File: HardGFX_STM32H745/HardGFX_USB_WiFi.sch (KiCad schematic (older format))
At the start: 24 parts, among them J1 UART, J7 47590-0001, J8 JTAG, J9 Boot Option, Q1 BSR14, SW1 SW_MEC_5E, U10 ESP32-WROOM-32E_(4MB), U8 STMPS2151STR, U9 USBLC6-4SC6

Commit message: Add Info folder that contain data about reference design, datasheet component of references.
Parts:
- U10: Digikey# (none) -> 1965-ESP32-WROOM-32E(4MBHIGHTEMP)TR-ND; Manf# (none) -> ESP32-WROOM-32E (4MB HIGH TEMP)
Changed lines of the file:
@@
 F 6 "1.1" H 3350 4000 50  0001 L BNN "PARTREV"
 F 7 "3.25mm" H 3350 4000 50  0001 L BNN "MAXIMUM_PACKAGE_HEIGHT"
+F 8 "1965-ESP32-WROOM-32E(4MBHIGHTEMP)TR-ND" H 3350 4000 50  0001 C CNN "Digikey#"
+F 9 "ESP32-WROOM-32E (4MB HIGH TEMP)" H 3350 4000 50  0001 C CNN "Manf#"
 	1    3350 4000
 	1    0    0    -1

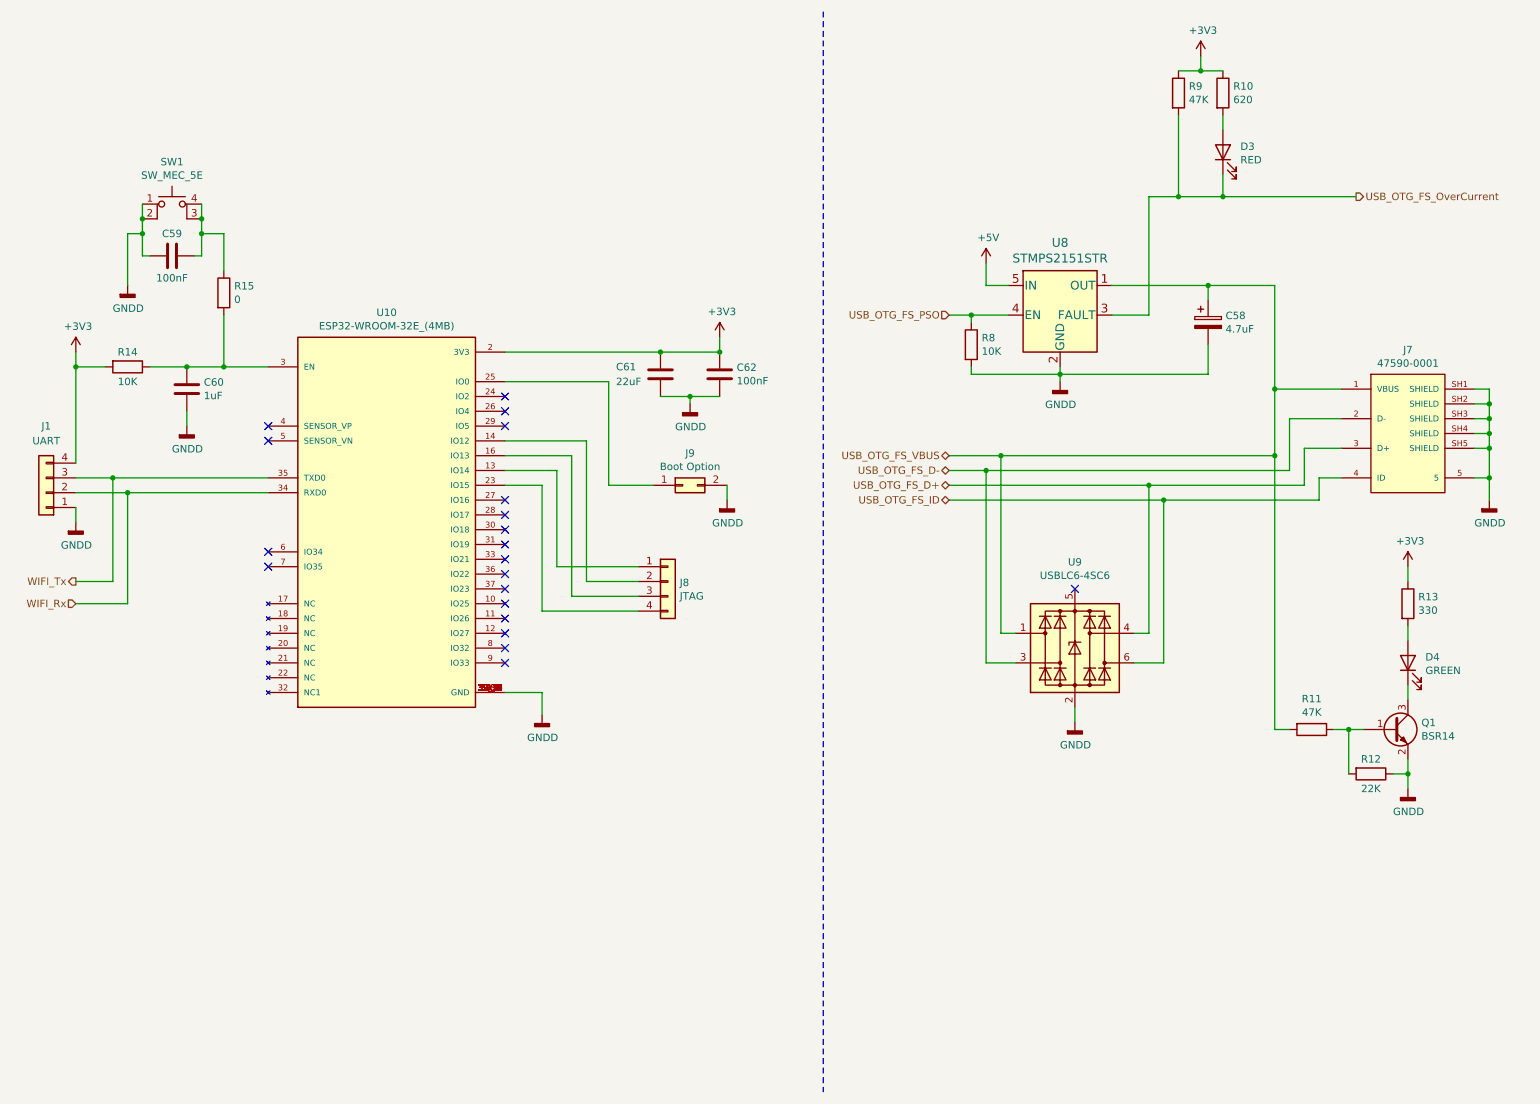
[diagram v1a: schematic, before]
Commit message: Filling field for do BOM with Kicost  and create proyect on IDE to start setting peripheral in MCU
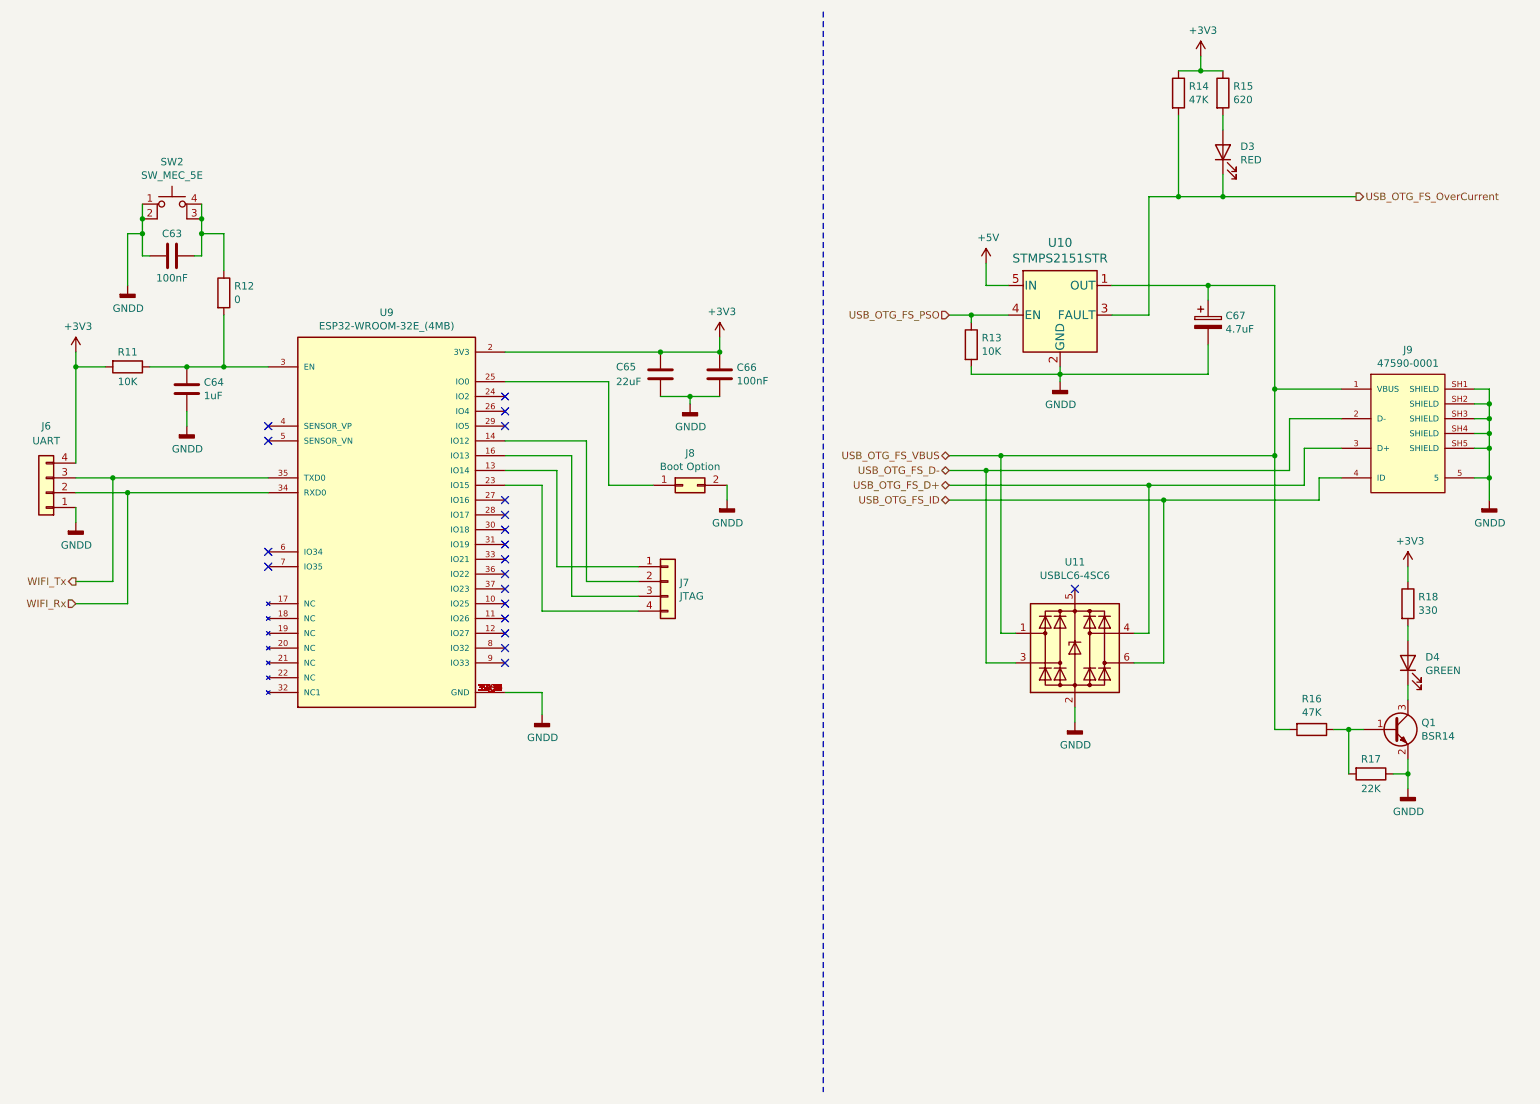
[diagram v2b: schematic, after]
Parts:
- D3: Digikey# (none) -> 732-5030-1-ND; MANUFACTURER (none) -> Wurth Elektronik; Manf# (none) -> 156120RS75000; Mouser# (none) -> 710-156120RS75000
- D4: Digikey# (none) -> 732-5032-1-ND; MANUFACTURER (none) -> Wurth Elektronik; Manf# (none) -> 156120VS75000; Mouser# (none) -> 710-156120VS75000
- SW2: renamed from SW1; footprint Button_Switch_SMD:SW_MEC_5GSH9 -> (none); Digikey# (none) -> 732-7022-1-ND; MANUFACTURER (none) -> Wurth Elektronik; Manf# (none) -> 430481025816; Mouser# (none) -> 710-430481025816
- U10: renamed from U8; Digikey# (none) -> 497-6934-1-ND; MANUFACTURER (none) -> STMicroelectronics; Manf# (none) -> STMPS2151STR; Mouser# (none) -> 511-STMPS2151STR
- U11: renamed from U9; Digikey# (none) -> 497-4492-1-ND; MANUFACTURER (none) -> STMicroelectronics; Manf# (none) -> USBLC6-4SC6; Mouser# (none) -> 511-USBLC6-4SC6
- U9: renamed from U10; Mouser# (none) -> 356-ESP32WRM320EH3PS
- renumbered C59 to C63, C60 to C64, C61 to C65, C62 to C66, C58 to C67, J1 to J6, J8 to J7, J9 to J8, J7 to J9, R14 to R11, R15 to R12, R8 to R13, R9 to R14, R10 to R15, R11 to R16, R12 to R17, R13 to R18

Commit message: I filled more component to Kicost script
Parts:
- J6, J7: Digikey# (none) -> 54101-G1004LF-ND; MANUFACTURER (none) -> Amphenol FCI; Manf# (none) -> 54101-G1004LF; Mouser# (none) -> 649-54101-G1004LF
- J8: Digikey# (none) -> 54101-S0802LF-ND; MANUFACTURER (none) -> Amphenol FCI; Manf# (none) -> 54101-S0802LF; Mouser# (none) -> 649-54101-S0802LF
- J9: Digikey# (none) -> 2266-47590-0001-ND; MANUFACTURER MOLEX INC -> Molex; Manf# (none) -> 47590-0001; Mouser# (none) -> 538-47590-0001
- Q1: Digikey# (none) -> BSR14CT-ND; MANUFACTURER (none) -> onsemi / Fairchild; Manf# (none) -> BSR14; Mouser# (none) -> 512-BSR14
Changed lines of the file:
@@
 Sheet 7 8
 Title "USB OTG and Wi-Fi"
-Date "2021-08-22"
+Date "2021-08-24"
 Rev "Rev. 1"
 Comp "HardGFX"
@@
 F 1 "47590-0001" H 10250 3824 50  0000 C CNN
 F 2 "Connector_USB:USB_Micro-AB_Molex_47590-0001" H 9950 2600 50  0001 L BNN
-F 3 "https://ar.mouser.com/datasheet/2/276/0475900001_IO_CONNECTORS-704847.pdf" H 10200 3350 50  0001 L BNN
-F 4 "MOLEX INC" H 10100 2400 50  0001 L BNN "MANUFACTURER"
+F 3 "https://www.molex.com/webdocs/datasheets/pdf/en-us/0475900001_IO_CONNECTORS.pdf" H 10200 3350 50  0001 L BNN
+F 4 "Molex" H 10100 2400 50  0001 L BNN "MANUFACTURER"
 F 5 "Manufacturer Recommendations" H 9750 2700 50  0001 L BNN "STANDARD"
 F 6 "B1" H 10250 2500 50  0001 L BNN "PARTREV"
+F 7 "2266-47590-0001-ND" H 10200 3350 50  0001 C CNN "Digikey#"
+F 8 "47590-0001" H 10200 3350 50  0001 C CNN "Manf#"
+F 9 "538-47590-0001" H 10200 3350 50  0001 C CNN "Mouser#"
 	1    10200 3350
 	1    0    0    -1
@@
 F 1 "Boot Option" H 5400 3826 50  0000 C CNN
 F 2 "Connector_PinHeader_2.54mm:PinHeader_2x01_P2.54mm_Vertical" H 5350 3700 50  0001 C CNN
-F 3 "~" H 5350 3700 50  0001 C CNN
+F 3 "https://cdn.amphenol-icc.com/media/wysiwyg/files/drawing/54101.pdf" H 5350 3700 50  0001 C CNN
+F 4 "54101-S0802LF-ND" H 5350 3700 50  0001 C CNN "Digikey#"
+F 5 "Amphenol FCI" H 5350 3700 50  0001 C CNN "MANUFACTURER"
+F 6 "54101-S0802LF" H 5350 3700 50  0001 C CNN "Manf#"
+F 7 "649-54101-S0802LF" H 5350 3700 50  0001 C CNN "Mouser#"
 	1    5350 3700
 	1    0    0    -1
@@
 F 1 "UART" H 1050 3400 50  0000 C CNN
 F 2 "Connector_Molex:Molex_KK-254_AE-6410-04A_1x04_P2.54mm_Vertical" H 1050 3750 50  0001 C CNN
-F 3 "~" H 1050 3750 50  0001 C CNN
+F 3 "https://cdn.amphenol-icc.com/media/wysiwyg/files/drawing/54101.pdf" H 1050 3750 50  0001 C CNN
+F 4 "54101-G1004LF-ND" H 1050 3750 50  0001 C CNN "Digikey#"
+F 5 "Amphenol FCI" H 1050 3750 50  0001 C CNN "MANUFACTURER"
+F 6 "54101-G1004LF" H 1050 3750 50  0001 C CNN "Manf#"
+F 7 "649-54101-G1004LF" H 1050 3750 50  0001 C CNN "Mouser#"
 	1    1050 3750
 	-1   0    0    1
@@
 F 1 "JTAG" H 5330 4251 50  0000 L CNN
 F 2 "Connector_Molex:Molex_KK-254_AE-6410-04A_1x04_P2.54mm_Vertical" H 5250 4350 50  0001 C CNN
-F 3 "~" H 5250 4350 50  0001 C CNN
+F 3 "https://cdn.amphenol-icc.com/media/wysiwyg/files/drawing/54101.pdf" H 5250 4350 50  0001 C CNN
+F 4 "54101-G1004LF-ND" H 5250 4350 50  0001 C CNN "Digikey#"
+F 5 "Amphenol FCI" H 5250 4350 50  0001 C CNN "MANUFACTURER"
+F 6 "54101-G1004LF" H 5250 4350 50  0001 C CNN "Manf#"
+F 7 "649-54101-G1004LF" H 5250 4350 50  0001 C CNN "Mouser#"
 	1    5250 4350
 	1    0    0    -1
@@
 F 1 "BSR14" H 10341 5305 50  0000 L CNN
 F 2 "Package_TO_SOT_SMD:SOT-23" H 10350 5450 50  0001 C CNN
-F 3 "https://ar.mouser.com/datasheet/2/308/1/BSR14_D-2310224.pdf" H 10150 5350 50  0001 C CNN
+F 3 "https://www.onsemi.com/pdf/datasheet/bsr14-d.pdf" H 10150 5350 50  0001 C CNN
+F 4 "BSR14CT-ND" H 10150 5350 50  0001 C CNN "Digikey#"
+F 5 "onsemi / Fairchild" H 10150 5350 50  0001 C CNN "MANUFACTURER"
+F 6 "BSR14 " H 10150 5350 50  0001 C CNN "Manf#"
+F 7 "512-BSR14" H 10150 5350 50  0001 C CNN "Mouser#"
 	1    10150 5350
 	1    0    0    -1

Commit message: Almost I end to fill Kicost field on schematics.
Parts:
- C63, C66: Digikey# (none) -> 311-1088-1-ND; MANUFACTURER (none) -> YAGEO; Manf# (none) -> CC0603KRX7R7BB104; Mouser# (none) -> 603-CC603KRX7R7BB104
- C64: Digikey# (none) -> 311-1444-1-ND; MANUFACTURER (none) -> YAGEO; Manf# (none) -> CC0603KRX5R7BB105; Mouser# (none) -> 603-CC603KRX5R7BB105
- C67: Digikey# (none) -> 718-595D475X9016A2TCT-ND; MANUFACTURER (none) -> Vishay / Sprague; Manf# (none) -> 595D475X9016A2T; Mouser# (none) -> 74-595D475X9016A2T
- R11, R13: Digikey# (none) -> 311-10.0KHRCT-ND; MANUFACTURER (none) -> YAGEO; Manf# (none) -> RC0603FR-0710KL; Mouser# (none) -> 603-RC0603FR-0710KL
- R12: Digikey# (none) -> PMR03EZPJ000-ND; MANUFACTURER (none) -> ROHM Semiconductor; Manf# (none) -> PMR03EZPJ000; Mouser# (none) -> 755-PMR03EZPJ000
- R14, R16: Digikey# (none) -> 311-47.0KHRCT-ND; MANUFACTURER (none) -> YAGEO; Manf# (none) -> RC0603FR-0747KL; Mouser# (none) -> 603-RC0603FR-0747KL
- R15: Digikey# (none) -> 311-620HRCT-ND; MANUFACTURER (none) -> YAGEO; Manf# (none) -> RC0603FR-07620RL; Mouser# (none) -> 603-RC0603FR-07620RL
- R17: Digikey# (none) -> 311-22.0KHRCT-ND; MANUFACTURER (none) -> YAGEO; Manf# (none) -> RC0603FR-0722KL; Mouser# (none) -> 603-RC0603FR-0722KL
- R18: Digikey# (none) -> 311-330HRCT-ND; MANUFACTURER (none) -> YAGEO; Manf# (none) -> RC0603FR-07330RL; Mouser# (none) -> 603-RC0603FR-07330RL
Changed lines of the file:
@@
 Sheet 7 8
 Title "USB OTG and Wi-Fi"
-Date "2021-08-24"
+Date "2021-08-25"
 Rev "Rev. 1"
 Comp "HardGFX"
@@
 F 1 "10K" H 7370 2705 50  0000 L CNN
 F 2 "" V 7230 2750 50  0001 C CNN
-F 3 "~" H 7300 2750 50  0001 C CNN
+F 3 "https://www.yageo.com/upload/media/product/productsearch/datasheet/rchip/PYu-RC_Group_51_RoHS_L_11.pdf" H 7300 2750 50  0001 C CNN
+F 4 "311-10.0KHRCT-ND" H 7300 2750 50  0001 C CNN "Digikey#"
+F 5 "YAGEO" H 7300 2750 50  0001 C CNN "MANUFACTURER"
+F 6 "RC0603FR-0710KL" H 7300 2750 50  0001 C CNN "Manf#"
+F 7 "603-RC0603FR-0710KL" H 7300 2750 50  0001 C CNN "Mouser#"
 	1    7300 2750
 	1    0    0    -1
@@
 F 1 "4.7uF" H 9018 2555 50  0000 L CNN
 F 2 "595D475X9016A2T:595D475X9016A2T" H 8938 2450 50  0001 C CNN
-F 3 "https://ar.mouser.com/datasheet/2/427/595d-1763504.pdf" H 8900 2600 50  0001 C CNN
+F 3 "https://www.vishay.com/docs/40007/595d.pdf" H 8900 2600 50  0001 C CNN
+F 4 "718-595D475X9016A2TCT-ND" H 8900 2600 50  0001 C CNN "Digikey#"
+F 5 "Vishay / Sprague" H 8900 2600 50  0001 C CNN "MANUFACTURER"
+F 6 "595D475X9016A2T" H 8900 2600 50  0001 C CNN "Manf#"
+F 7 "74-595D475X9016A2T" H 8900 2600 50  0001 C CNN "Mouser#"
 	1    8900 2600
 	1    0    0    -1
@@
 F 1 "47K" H 8770 1005 50  0000 L CNN
 F 2 "" V 8630 1050 50  0001 C CNN
-F 3 "~" H 8700 1050 50  0001 C CNN
+F 3 "https://www.yageo.com/upload/media/product/productsearch/datasheet/rchip/PYu-RC_Group_51_RoHS_L_11.pdf" H 8700 1050 50  0001 C CNN
+F 4 "311-47.0KHRCT-ND" H 8700 1050 50  0001 C CNN "Digikey#"
+F 5 "YAGEO" H 8700 1050 50  0001 C CNN "MANUFACTURER"
+F 6 "RC0603FR-0747KL" H 8700 1050 50  0001 C CNN "Manf#"
+F 7 "603-RC0603FR-0747KL" H 8700 1050 50  0001 C CNN "Mouser#"
 	1    8700 1050
 	1    0    0    -1
@@
 F 1 "620" H 9070 1005 50  0000 L CNN
 F 2 "" V 8930 1050 50  0001 C CNN
-F 3 "~" H 9000 1050 50  0001 C CNN
+F 3 "https://www.yageo.com/upload/media/product/productsearch/datasheet/rchip/PYu-RC_Group_51_RoHS_L_11.pdf" H 9000 1050 50  0001 C CNN
+F 4 "311-620HRCT-ND" H 9000 1050 50  0001 C CNN "Digikey#"
+F 5 "YAGEO" H 9000 1050 50  0001 C CNN "MANUFACTURER"
+F 6 "RC0603FR-07620RL" H 9000 1050 50  0001 C CNN "Manf#"
+F 7 "603-RC0603FR-07620RL" H 9000 1050 50  0001 C CNN "Mouser#"
 	1    9000 1050
 	1    0    0    -1
@@
 F 1 "330" H 10320 4455 50  0000 L CNN
 F 2 "" V 10180 4500 50  0001 C CNN
-F 3 "~" H 10250 4500 50  0001 C CNN
+F 3 "https://www.yageo.com/upload/media/product/productsearch/datasheet/rchip/PYu-RC_Group_51_RoHS_L_11.pdf" H 10250 4500 50  0001 C CNN
+F 4 "311-330HRCT-ND" H 10250 4500 50  0001 C CNN "Digikey#"
+F 5 "YAGEO" H 10250 4500 50  0001 C CNN "MANUFACTURER"
+F 6 "RC0603FR-07330RL" H 10250 4500 50  0001 C CNN "Manf#"
+F 7 "603-RC0603FR-07330RL" H 10250 4500 50  0001 C CNN "Mouser#"
 	1    10250 4500
 	1    0    0    -1
@@
 F 1 "22K" V 10100 5650 50  0000 C CNN
 F 2 "" V 9930 5650 50  0001 C CNN
-F 3 "~" H 10000 5650 50  0001 C CNN
+F 3 "https://www.yageo.com/upload/media/product/productsearch/datasheet/rchip/PYu-RC_Group_51_RoHS_L_11.pdf" H 10000 5650 50  0001 C CNN
+F 4 "311-22.0KHRCT-ND" H 10000 5650 50  0001 C CNN "Digikey#"
+F 5 "YAGEO" H 10000 5650 50  0001 C CNN "MANUFACTURER"
+F 6 "RC0603FR-0722KL" H 10000 5650 50  0001 C CNN "Manf#"
+F 7 "603-RC0603FR-0722KL" H 10000 5650 50  0001 C CNN "Mouser#"
 	1    10000 5650
 	0    1    1    0
@@
 F 1 "47K" V 9484 5350 50  0000 C CNN
 F 2 "" V 9530 5350 50  0001 C CNN
-F 3 "~" H 9600 5350 50  0001 C CNN
+F 3 "https://www.yageo.com/upload/media/product/productsearch/datasheet/rchip/PYu-RC_Group_51_RoHS_L_11.pdf" H 9600 5350 50  0001 C CNN
+F 4 "311-47.0KHRCT-ND" H 9600 5350 50  0001 C CNN "Digikey#"
+F 5 "YAGEO" H 9600 5350 50  0001 C CNN "MANUFACTURER"
+F 6 "RC0603FR-0747KL" H 9600 5350 50  0001 C CNN "Manf#"
+F 7 "603-RC0603FR-0747KL" H 9600 5350 50  0001 C CNN "Mouser#"
 	1    9600 5350
 	0    1    1    0
@@
 F 1 "10K" V 1700 2900 50  0000 C CNN
 F 2 "" V 1530 2900 50  0001 C CNN
-F 3 "~" H 1600 2900 50  0001 C CNN
+F 3 "https://www.yageo.com/upload/media/product/productsearch/datasheet/rchip/PYu-RC_Group_51_RoHS_L_11.pdf" H 1600 2900 50  0001 C CNN
+F 4 "311-10.0KHRCT-ND" H 1600 2900 50  0001 C CNN "Digikey#"
+F 5 "YAGEO" H 1600 2900 50  0001 C CNN "MANUFACTURER"
+F 6 "RC0603FR-0710KL" H 1600 2900 50  0001 C CNN "Manf#"
+F 7 "603-RC0603FR-0710KL" H 1600 2900 50  0001 C CNN "Mouser#"
 	1    1600 2900
 	0    1    1    0
@@
 F 1 "1uF" H 2115 3005 50  0000 L CNN
 F 2 "Capacitor_SMD:C_0603_1608Metric" H 2038 2900 50  0001 C CNN
-F 3 "https://ar.mouser.com/datasheet/2/447/yago_s_a0011397150_1-2286655.pdf" H 2000 3050 50  0001 C CNN
+F 3 "https://www.yageo.com/upload/media/product/productsearch/datasheet/mlcc/UPY-GPHC_X5R_4V-to-50V_26.pdf" H 2000 3050 50  0001 C CNN
+F 4 "311-1444-1-ND" H 2000 3050 50  0001 C CNN "Digikey#"
+F 5 "YAGEO" H 2000 3050 50  0001 C CNN "MANUFACTURER"
+F 6 "CC0603KRX5R7BB105" H 2000 3050 50  0001 C CNN "Manf#"
+F 7 "603-CC603KRX5R7BB105" H 2000 3050 50  0001 C CNN "Mouser#"
 	1    2000 3050
 	1    0    0    -1
@@
 F 1 "100nF" V 2050 2150 50  0000 C CNN
 F 2 "Capacitor_SMD:C_0603_1608Metric" H 1938 2000 50  0001 C CNN
-F 3 "https://ar.mouser.com/datasheet/2/447/UPY_GPHC_X7R_6_3V_to_50V_20-1995650.pdf" H 1900 2150 50  0001 C CNN
+F 3 "https://www.yageo.com/upload/media/product/productsearch/datasheet/mlcc/UPY-GPHC_X7R_6.3V-to-50V_18.pdf" H 1900 2150 50  0001 C CNN
+F 4 "311-1088-1-ND" H 1900 2150 50  0001 C CNN "Digikey#"
+F 5 "YAGEO" H 1900 2150 50  0001 C CNN "MANUFACTURER"
+F 6 "CC0603KRX7R7BB104" H 1900 2150 50  0001 C CNN "Manf#"
+F 7 "603-CC603KRX7R7BB104" H 1900 2150 50  0001 C CNN "Mouser#"
 	1    1900 2150
 	0    1    1    0
@@
 F 1 "0" H 2320 2355 50  0000 L CNN
 F 2 "" V 2180 2400 50  0001 C CNN
-F 3 "~" H 2250 2400 50  0001 C CNN
+F 3 "https://ar.mouser.com/datasheet/2/348/pmr_jpw_e-1874603.pdf" H 2250 2400 50  0001 C CNN
+F 4 "PMR03EZPJ000-ND" H 2250 2400 50  0001 C CNN "Digikey#"
+F 5 "ROHM Semiconductor" H 2250 2400 50  0001 C CNN "MANUFACTURER"
+F 6 "PMR03EZPJ000" H 2250 2400 50  0001 C CNN "Manf#"
+F 7 "755-PMR03EZPJ000" H 2250 2400 50  0001 C CNN "Mouser#"
 	1    2250 2400
 	1    0    0    -1
@@
 F 1 "100nF" H 5715 2905 50  0000 L CNN
 F 2 "Capacitor_SMD:C_0603_1608Metric" H 5638 2800 50  0001 C CNN
-F 3 "https://ar.mouser.com/datasheet/2/447/UPY_GPHC_X7R_6_3V_to_50V_20-1995650.pdf" H 5600 2950 50  0001 C CNN
+F 3 "https://www.yageo.com/upload/media/product/productsearch/datasheet/mlcc/UPY-GPHC_X7R_6.3V-to-50V_18.pdf" H 5600 2950 50  0001 C CNN
+F 4 "311-1088-1-ND" H 5600 2950 50  0001 C CNN "Digikey#"
+F 5 "YAGEO" H 5600 2950 50  0001 C CNN "MANUFACTURER"
+F 6 "CC0603KRX7R7BB104" H 5600 2950 50  0001 C CNN "Manf#"
+F 7 "603-CC603KRX7R7BB104" H 5600 2950 50  0001 C CNN "Mouser#"
 	1    5600 2950
 	1    0    0    -1
